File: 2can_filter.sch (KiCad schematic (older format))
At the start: 17 parts, among them J3 USB mini-B SMD, J4 NOT_FITTED_SWD_Conn_01x04_Male, U5 STM32F105RBTx, U6 TJA1040T, U7 TJA1040T, Y1 Crystal KX-13 25MHz

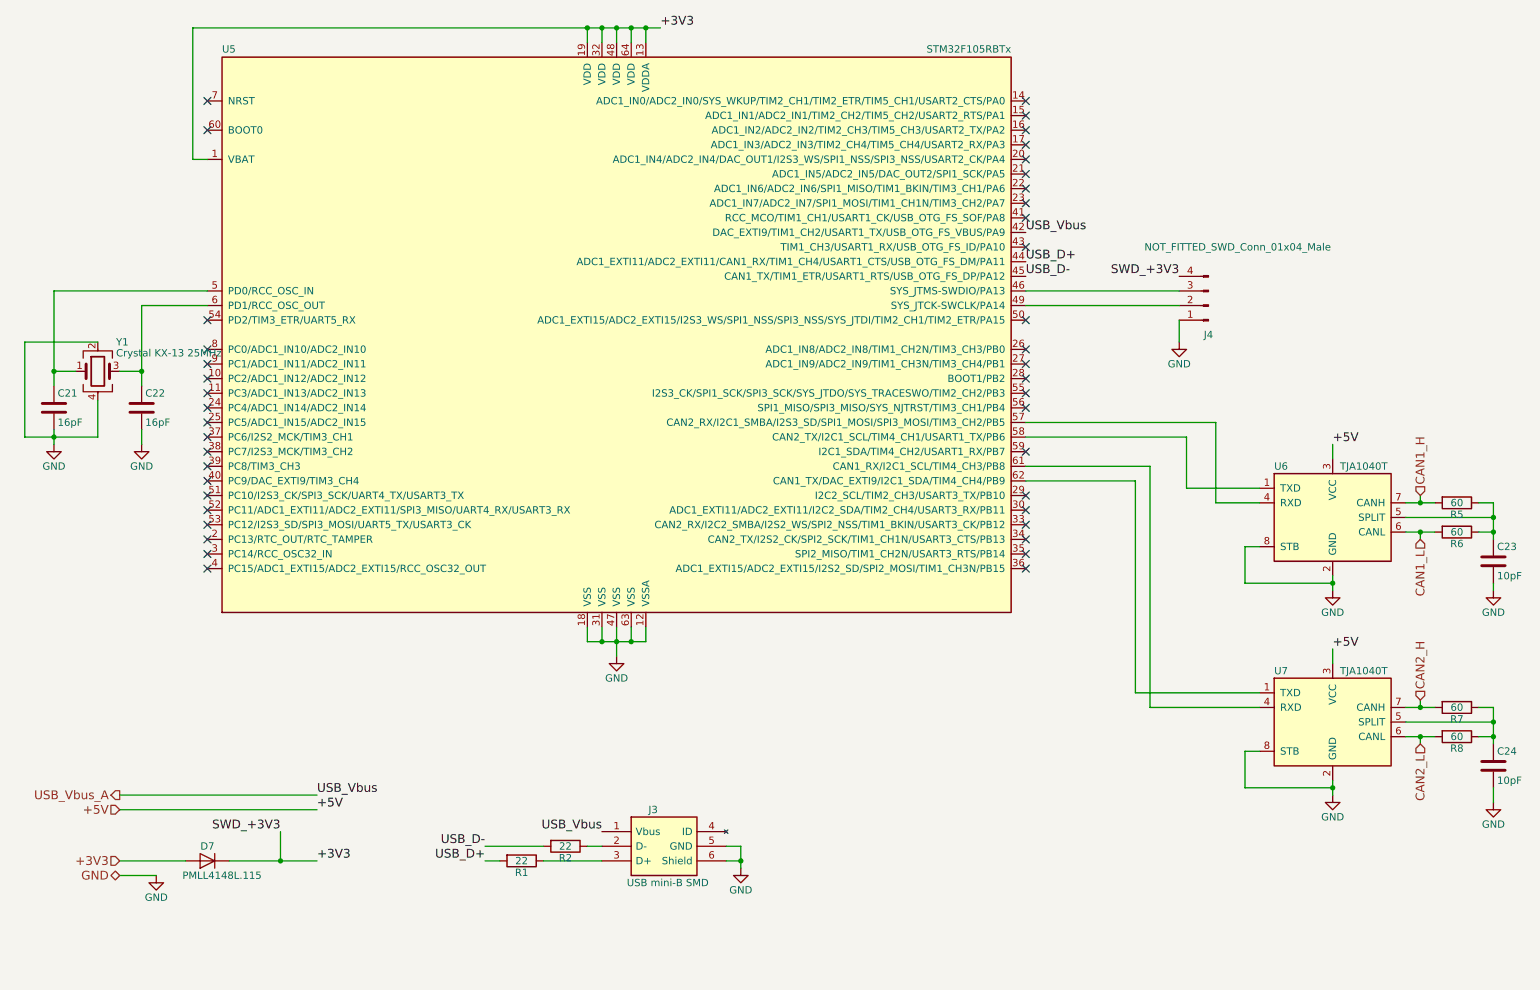
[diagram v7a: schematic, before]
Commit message: redone shematic of power supply, fix usb_vbus and swd diods connections, change mcu capacitors connections
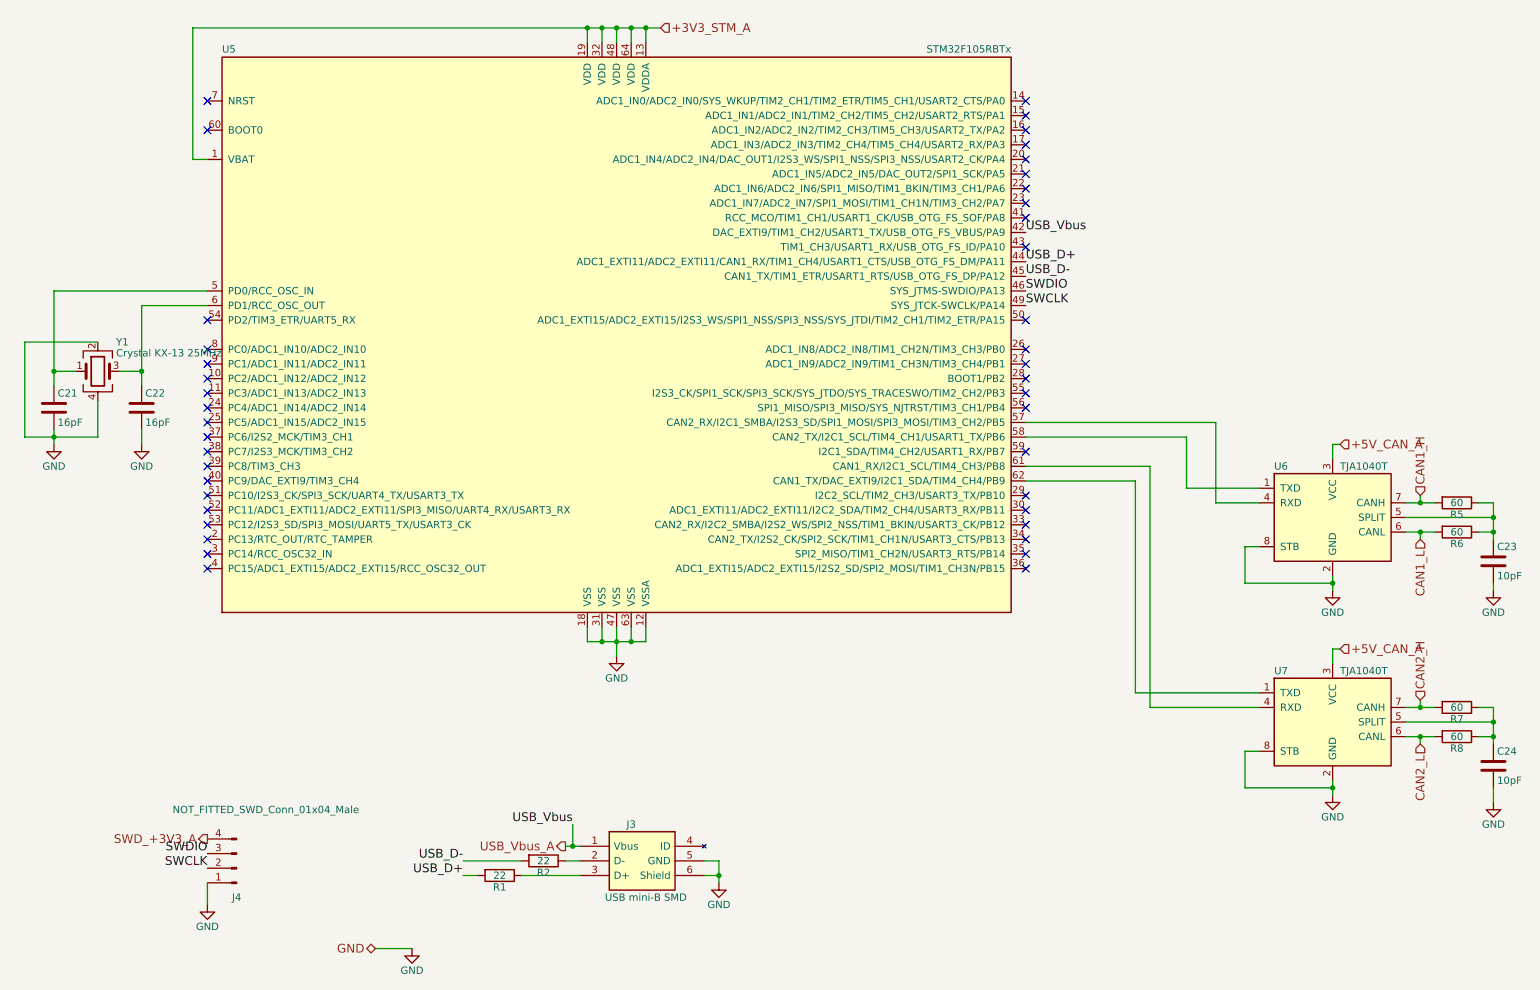
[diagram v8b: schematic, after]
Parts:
- removed D7: PMLL4148L.115, Diodes_SMD:D_SC-80, symbol D
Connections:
- net SWCLK: now reaches J4.2 (Pin_2), U5.49 (SYS_JTCK-SWCLK/PA14)
- net SWDIO: now reaches J4.3 (Pin_3), U5.46 (SYS_JTMS-SWDIO/PA13)
- net +3V3 renamed +3V3_STM_A
- net +3V3_STM_A: no longer J4.4 (Pin_4)
- net +5V renamed +5V_CAN_A
- new net SWD_+3V3_A: J4.4 (Pin_4)
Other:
- moved on the sheet: J3, J4, R1, R2
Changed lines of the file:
@@
 $Descr A4 11693 8268
 encoding utf-8
-Sheet 3 4
+Sheet 2 4
 Title "Instrument Cluster"
 Date "2017-11-11"
@@
 	1    0    0    -1
 $EndComp
-Text HLabel 1500 6500 0    60   Input ~ 0
-+3V3
+Text HLabel 5200 800  2    60   Input ~ 0
++3V3_STM_A
 Text HLabel 10400 4000 1    60   Input ~ 0
 CAN1_H
@@
 	1    0    0    -1
 $EndComp
-Wire Wire Line
-	1500 6500 1950 6500
 $Comp
 L C C23
@@
 	10400 4000 10400 4050
 Connection ~ 10400 4050
-Text HLabel 1500 6600 0    60   BiDi ~ 0
+Text HLabel 3250 7100 0    60   BiDi ~ 0
 GND
 Wire Wire Line
-	1500 6600 1750 6600
-Text Label 9800 5050 0    60   ~ 0
-+5V
-Text Label 5200 800  0    60   ~ 0
-+3V3
-$Comp
-L GND #PWR021
+	3250 7100 3500 7100
+$Comp
+L GND #PWR06
 U 1 1 5A09EB1D
-P 1750 6600
-F 0 "#PWR021" H 1750 6350 50  0001 C CNN
-F 1 "GND" H 1750 6450 50  0000 C CNN
-F 2 "" H 1750 6600 50  0001 C CNN
-F 3 "" H 1750 6600 50  0001 C CNN
-	1    1750 6600
+P 3500 7100
+F 0 "#PWR06" H 3500 6850 50  0001 C CNN
+F 1 "GND" H 3500 6950 50  0000 C CNN
+F 2 "" H 3500 7100 50  0001 C CNN
+F 3 "" H 3500 7100 50  0001 C CNN
+	1    3500 7100
 	1    0    0    -1
 $EndComp
@@
 Connection ~ 4800 5000
 $Comp
-L GND #PWR022
+L GND #PWR07
 U 1 1 5A09EB1E
 P 4900 5100
-F 0 "#PWR022" H 4900 4850 50  0001 C CNN
+F 0 "#PWR07" H 4900 4850 50  0001 C CNN
 F 1 "GND" H 4900 4950 50  0000 C CNN
 F 2 "" H 4900 5100 50  0001 C CNN
@@
 	1    0    0    -1
 $EndComp
-Text Label 2850 6500 0    60   ~ 0
-+3V3
 Wire Wire Line
 	10300 4250 10500 4250
@@
 Connection ~ 10400 5650
 Wire Wire Line
-	9800 5050 9800 5150
-Wire Wire Line
 	9800 3750 9800 3650
-Text Label 9800 3650 0    60   ~ 0
-+5V
 Wire Wire Line
 	8450 5350 9300 5350
@@
 	9200 4350 9300 4350
 $Comp
-L GND #PWR023
+L GND #PWR08
 U 1 1 5A048D0B
 P 9800 4650
-F 0 "#PWR023" H 9800 4400 50  0001 C CNN
+F 0 "#PWR08" H 9800 4400 50  0001 C CNN
 F 1 "GND" H 9800 4500 50  0000 C CNN
 F 2 "" H 9800 4650 50  0001 C CNN
@@
 	9800 4550 9800 4650
 $Comp
-L GND #PWR024
+L GND #PWR09
 U 1 1 5A09EB24
 P 10900 4650
-F 0 "#PWR024" H 10900 4400 50  0001 C CNN
+F 0 "#PWR09" H 10900 4400 50  0001 C CNN
 F 1 "GND" H 10900 4500 50  0000 C CNN
 F 2 "" H 10900 4650 50  0001 C CNN
@@
 	9200 5750 9300 5750
 $Comp
-L GND #PWR025
+L GND #PWR010
 U 1 1 5A09EB28
 P 9800 6050
-F 0 "#PWR025" H 9800 5800 50  0001 C CNN
+F 0 "#PWR010" H 9800 5800 50  0001 C CNN
 F 1 "GND" H 9800 5900 50  0000 C CNN
 F 2 "" H 9800 6050 50  0001 C CNN
@@
 	9800 5950 9800 6050
 $Comp
-L GND #PWR026
+L GND #PWR011
 U 1 1 5A0491F4
 P 10900 6100
-F 0 "#PWR026" H 10900 5850 50  0001 C CNN
+F 0 "#PWR011" H 10900 5850 50  0001 C CNN
 F 1 "GND" H 10900 5950 50  0000 C CNN
 F 2 "" H 10900 6100 50  0001 C CNN
@@
 	10900 6000 10900 6100
 $Comp
-L D D7
-U 1 1 5A0494E2
-P 2100 6500
-F 0 "D7" H 2100 6400 50  0000 C CNN
-F 1 "PMLL4148L.115" H 2000 6600 50  0000 C CNN
-F 2 "Diodes_SMD:D_SC-80" H 2100 6500 50  0001 C CNN
-F 3 "" H 2100 6500 50  0001 C CNN
-	1    2100 6500
-	-1   0    0    1
-$EndComp
-$Comp
 L Conn_01x04_Male J4
 U 1 1 5A0495DE
-P 8950 2700
-F 0 "J4" H 8950 2900 50  0000 C CNN
-F 1 "NOT_FITTED_SWD_Conn_01x04_Male" H 8750 2300 50  0000 C CNN
-F 2 "Pin_Headers:Pin_Header_Straight_1x04_Pitch2.54mm" H 8950 2700 50  0001 C CNN
-F 3 "" H 8950 2700 50  0001 C CNN
-	1    8950 2700
+P 2300 6550
+F 0 "J4" H 2300 6750 50  0000 C CNN
+F 1 "NOT_FITTED_SWD_Conn_01x04_Male" H 2100 6150 50  0000 C CNN
+F 2 "Pin_Headers:Pin_Header_Straight_1x04_Pitch2.54mm" H 2300 6550 50  0001 C CNN
+F 3 "" H 2300 6550 50  0001 C CNN
+	1    2300 6550
 	-1   0    0    1
 $EndComp
 Wire Wire Line
-	8750 2700 7700 2700
-Wire Wire Line
-	7700 2600 8750 2600
-Wire Wire Line
-	8750 2950 8750 2800
-$Comp
-L GND #PWR027
+	2100 6800 2100 6650
+$Comp
+L GND #PWR012
 U 1 1 5A0498E0
-P 8750 2950
-F 0 "#PWR027" H 8750 2700 50  0001 C CNN
-F 1 "GND" H 8750 2800 50  0000 C CNN
-F 2 "" H 8750 2950 50  0001 C CNN
-F 3 "" H 8750 2950 50  0001 C CNN
-	1    8750 2950
-	1    0    0    -1
-$EndComp
-Text Label 8750 2500 2    60   ~ 0
-SWD_+3V3
-Text Label 2600 6300 2    60   ~ 0
-SWD_+3V3
-Wire Wire Line
-	2250 6500 2850 6500
-Wire Wire Line
-	2600 6300 2600 6500
-Connection ~ 2600 6500
+P 2100 6800
+F 0 "#PWR012" H 2100 6550 50  0001 C CNN
+F 1 "GND" H 2100 6650 50  0000 C CNN
+F 2 "" H 2100 6800 50  0001 C CNN
+F 3 "" H 2100 6800 50  0001 C CNN
+	1    2100 6800
+	1    0    0    -1
+$EndComp
 $Comp
 L C C22
@@
 $EndComp
 $Comp
-L GND #PWR028
+L GND #PWR013
 U 1 1 5A04A703
 P 1050 3650
-F 0 "#PWR028" H 1050 3400 50  0001 C CNN
+F 0 "#PWR013" H 1050 3400 50  0001 C CNN
 F 1 "GND" H 1050 3500 50  0000 C CNN
 F 2 "" H 1050 3650 50  0001 C CNN
@@
 $EndComp
 $Comp
-L GND #PWR029
+L GND #PWR014
 U 1 1 5A04A747
 P 1650 3650
-F 0 "#PWR029" H 1650 3400 50  0001 C CNN
+F 0 "#PWR014" H 1650 3400 50  0001 C CNN
 F 1 "GND" H 1650 3500 50  0000 C CNN
 F 2 "" H 1650 3650 50  0001 C CNN
@@
 Connection ~ 1650 3150
 $Comp
-L GND #PWR030
+L GND #PWR015
 U 1 1 5A04B0EB
-P 5750 6550
-F 0 "#PWR030" H 5750 6300 50  0001 C CNN
-F 1 "GND" H 5750 6400 50  0000 C CNN
-F 2 "" H 5750 6550 50  0001 C CNN
-F 3 "" H 5750 6550 50  0001 C CNN
-	1    5750 6550
-	1    0    0    -1
-$EndComp
-Text Label 4000 6500 2    60   ~ 0
+P 5600 6650
+F 0 "#PWR015" H 5600 6400 50  0001 C CNN
+F 1 "GND" H 5600 6500 50  0000 C CNN
+F 2 "" H 5600 6650 50  0001 C CNN
+F 3 "" H 5600 6650 50  0001 C CNN
+	1    5600 6650
+	1    0    0    -1
+$EndComp
+Text Label 3850 6600 2    60   ~ 0
 USB_D+
-Text Label 4000 6400 2    60   ~ 0
+Text Label 3850 6500 2    60   ~ 0
 USB_D-
-Text Label 4800 6300 2    60   ~ 0
-USB_Vbus
 Text Label 7700 2400 0    60   ~ 0
 USB_D+
@@
 Wire Wire Line
 	8800 3600 8800 3950
-Text Label 2850 6050 0    60   ~ 0
-USB_Vbus
-Text HLabel 1500 6150 0    60   Input ~ 0
-+5V
-Wire Wire Line
-	1500 6150 2850 6150
-Text Label 2850 6150 0    60   ~ 0
-+5V
-Wire Wire Line
-	2850 6050 1500 6050
-Text HLabel 1500 6050 0    60   Output ~ 0
+Text HLabel 9850 3650 2    60   Input ~ 0
++5V_CAN_A
+Text HLabel 4550 6400 0    60   Output ~ 0
 USB_Vbus_A
 NoConn ~ 2100 2800
@@
 L 54819-0572 J3
 U 1 1 5A09A3F6
-P 4800 6300
-F 0 "J3" H 5150 6450 50  0000 C CNN
-F 1 "USB mini-B SMD" H 5250 5950 50  0000 C CNN
-F 2 "zulljon:USB_mini_B" H 5150 5850 50  0001 C CNN
-F 3 "http://www.molex.com/webdocs/datasheets/pdf/en-us/0548190572_IO_CONNECTORS.pdf" H 5150 5750 50  0001 C CNN
-F 4 "Surface mount onthego connector,1A 30V Molex On-The-Go Series Right Angle SMT Version 2.0 Type B Mini USB Connector Receptacle, 30 V, 1A" H 5150 5650 50  0001 C CNN "Description"
-F 5 "RS" H 5150 5550 50  0001 C CNN "Supplier_Name"
-F 6 "5151995P" H 5150 5450 50  0001 C CNN "RS Part Number"
-F 7 "Molex" H 5150 5350 50  0001 C CNN "Manufacturer_Name"
-F 8 "54819-0572" H 5150 5250 50  0001 C CNN "Manufacturer_Part_Number"
-F 9 "70266924" H 5150 5150 50  0001 C CNN "Allied_Number"
-	1    4800 6300
-	1    0    0    -1
-$EndComp
-Wire Wire Line
-	5650 6400 5750 6400
-Wire Wire Line
-	5750 6400 5750 6550
+P 4650 6400
+F 0 "J3" H 5000 6550 50  0000 C CNN
+F 1 "USB mini-B SMD" H 5100 6050 50  0000 C CNN
+F 2 "zulljon:USB_mini_B" H 5000 5950 50  0001 C CNN
+F 3 "http://www.molex.com/webdocs/datasheets/pdf/en-us/0548190572_IO_CONNECTORS.pdf" H 5000 5850 50  0001 C CNN
+F 4 "Surface mount onthego connector,1A 30V Molex On-The-Go Series Right Angle SMT Version 2.0 Type B Mini USB Connector Receptacle, 30 V, 1A" H 5000 5750 50  0001 C CNN "Description"
+F 5 "RS" H 5000 5650 50  0001 C CNN "Supplier_Name"
+F 6 "5151995P" H 5000 5550 50  0001 C CNN "RS Part Number"
+F 7 "Molex" H 5000 5450 50  0001 C CNN "Manufacturer_Name"
+F 8 "54819-0572" H 5000 5350 50  0001 C CNN "Manufacturer_Part_Number"
+F 9 "70266924" H 5000 5250 50  0001 C CNN "Allied_Number"
+	1    4650 6400
+	1    0    0    -1
+$EndComp
+Wire Wire Line
+	5500 6500 5600 6500
+Wire Wire Line
+	5600 6500 5600 6650
 $Comp
 L R R2
 U 1 1 5A0C2815
-P 4550 6400
-F 0 "R2" V 4630 6400 50  0000 C CNN
-F 1 "22" V 4550 6400 50  0000 C CNN
-F 2 "Resistors_SMD:R_0805" V 4480 6400 50  0001 C CNN
-F 3 "" H 4550 6400 50  0001 C CNN
-	1    4550 6400
+P 4400 6500
+F 0 "R2" V 4480 6500 50  0000 C CNN
+F 1 "22" V 4400 6500 50  0000 C CNN
+F 2 "Resistors_SMD:R_0805" V 4330 6500 50  0001 C CNN
+F 3 "" H 4400 6500 50  0001 C CNN
+	1    4400 6500
 	0    1    1    0
 $EndComp
@@
 L R R1
 U 1 1 5A0C28CE
-P 4250 6500
-F 0 "R1" V 4330 6500 50  0000 C CNN
-F 1 "22" V 4250 6500 50  0000 C CNN
-F 2 "Resistors_SMD:R_0805" V 4180 6500 50  0001 C CNN
-F 3 "" H 4250 6500 50  0001 C CNN
-	1    4250 6500
+P 4100 6600
+F 0 "R1" V 4180 6600 50  0000 C CNN
+F 1 "22" V 4100 6600 50  0000 C CNN
+F 2 "Resistors_SMD:R_0805" V 4030 6600 50  0001 C CNN
+F 3 "" H 4100 6600 50  0001 C CNN
+	1    4100 6600
 	0    1    1    0
 $EndComp
 Wire Wire Line
-	4000 6400 4400 6400
-Wire Wire Line
-	4700 6400 4800 6400
-Wire Wire Line
-	4800 6500 4400 6500
-Wire Wire Line
-	4100 6500 4000 6500
+	3850 6500 4250 6500
+Wire Wire Line
+	4550 6500 4650 6500
+Wire Wire Line
+	4650 6600 4250 6600
+Wire Wire Line
+	3950 6600 3850 6600
 $Comp
 L Crystal_GND24 Y1
@@
 	1350 3600 1350 3350
 Wire Wire Line
-	5650 6500 5750 6500
-Connection ~ 5750 6500
+	5500 6600 5600 6600
+Connection ~ 5600 6600
 Wire Wire Line
 	9200 4600 9800 4600
@@
 Wire Wire Line
 	9200 6000 9200 5750
+Text HLabel 2100 6350 0    60   Output ~ 0
+SWD_+3V3_A
+Text HLabel 9850 5050 2    60   Input ~ 0
++5V_CAN_A
+Wire Wire Line
+	9800 5150 9800 5050
+Wire Wire Line
+	9800 5050 9850 5050
+Wire Wire Line
+	9800 3650 9850 3650
+Text Label 7700 2600 0    60   ~ 0
+SWDIO
+Text Label 7700 2700 0    60   ~ 0
+SWCLK
+Text Label 2100 6450 2    60   ~ 0
+SWDIO
+Text Label 2100 6550 2    60   ~ 0
+SWCLK
+Text Label 4600 6250 2    60   ~ 0
+USB_Vbus
+Wire Wire Line
+	4600 6250 4600 6400
+Wire Wire Line
+	4550 6400 4650 6400
+Connection ~ 4600 6400
 $EndSCHEMATC
